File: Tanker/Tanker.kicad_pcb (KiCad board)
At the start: 2 copper layers, 47.6 x 18.8 mm, 1 part

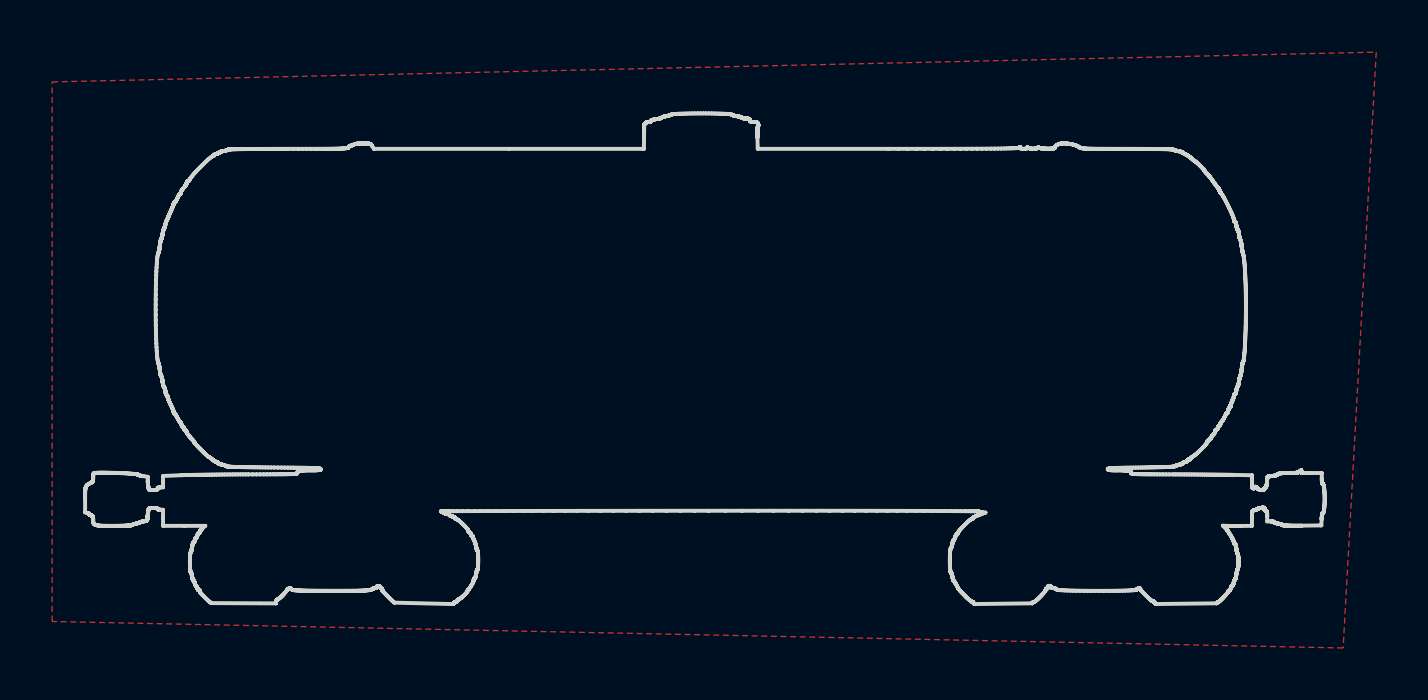
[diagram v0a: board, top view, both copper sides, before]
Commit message: Add & Align Pins
Add pins to all trains and set proper locations
Move RGB LEDs and resistors
Connect RGB LEDs to resistors and speaker to Arduino
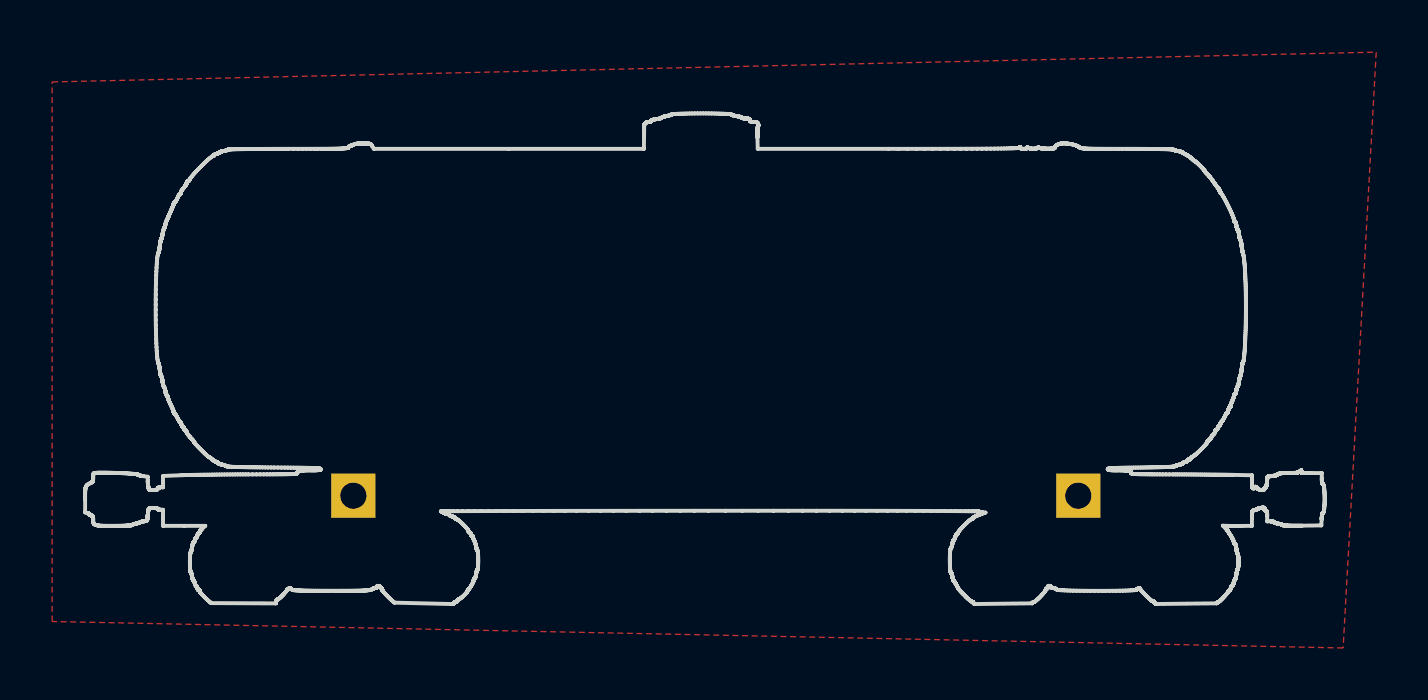
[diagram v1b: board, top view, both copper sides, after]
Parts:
- added MK1: Mounting_Hole_PAD, Pin_Headers:Pin_Header_Angled_1x01_Pitch2.54mm, B.Cu at (10.3, 95.8)
- added MK2: Mounting_Hole_PAD, Pin_Headers:Pin_Header_Angled_1x01_Pitch2.54mm, B.Cu at (38.1, 95.8)
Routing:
- added copper zone on F.Cu, net Net-(MK2-Pad1)
- removed copper zone on F.Cu, net (none)
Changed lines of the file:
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@@
-(kicad_pcb (version 20171130) (host pcbnew 5.0.0-rc2-dev-unknown-bf135b0~64~ubuntu16.04.1)
+(kicad_pcb (version 20171130) (host pcbnew 5.0.0-rc2-dev-unknown-1ac905d~64~ubuntu16.04.1)
   (general
     (thickness 1.6)
@@
     (tracks 0)
     (zones 0)
-    (modules 1)
-    (nets 1)
+    (modules 3)
+    (nets 2)
   )
   (page A4)
@@
   )
   (net 0 "")
+  (net 1 "Net-(MK2-Pad1)")
   (net_class Default "This is the default net class."
     (clearance 0.2)
@@
       (xy -1.887905 -6.02479) (xy -0.5608 -6.024797) (xy 0.777796 -6.024789)) (layer F.Mask) (width 0.01))
   )
+  (module Pin_Headers:Pin_Header_Angled_1x01_Pitch2.54mm (layer B.Cu)
+    (at 10.287 95.758 270)
+    (descr "Through hole angled pin header, 1x01, 2.54mm pitch, 6mm pin length, single row")
+    (tags "Through hole angled pin header THT 1x01 2.54mm single row")
+    (fp_text reference MK1 (at 4.385 2.27 270) (layer B.SilkS) hide
+      (effects (font (size 1 1) (thickness 0.15)) (justify mirror))
+    )
+    (fp_text value Mounting_Hole_PAD (at 4.385 -2.27 270) (layer B.Fab)
+      (effects (font (size 1 1) (thickness 0.15)) (justify mirror))
+    )
+    (fp_line (start 2.135 1.27) (end 4.04 1.27) (layer B.Fab) (width 0.1))
+    (fp_line (start 4.04 1.27) (end 4.04 -1.27) (layer B.Fab) (width 0.1))
+    (fp_line (start 4.04 -1.27) (end 1.5 -1.27) (layer B.Fab) (width 0.1))
+    (fp_line (start 1.5 -1.27) (end 1.5 0.635) (layer B.Fab) (width 0.1))
+    (fp_line (start 1.5 0.635) (end 2.135 1.27) (layer B.Fab) (width 0.1))
+    (fp_line (start -0.32 0.32) (end 1.5 0.32) (layer B.Fab) (width 0.1))
+    (fp_line (start -0.32 0.32) (end -0.32 -0.32) (layer B.Fab) (width 0.1))
+    (fp_line (start -0.32 -0.32) (end 1.5 -0.32) (layer B.Fab) (width 0.1))
+    (fp_line (start 4.04 0.32) (end 10.04 0.32) (layer B.Fab) (width 0.1))
+    (fp_line (start 10.04 0.32) (end 10.04 -0.32) (layer B.Fab) (width 0.1))
+    (fp_line (start 4.04 -0.32) (end 10.04 -0.32) (layer B.Fab) (width 0.1))
+    (fp_line (start 1.44 1.33) (end 1.44 -1.33) (layer B.SilkS) (width 0.12))
+    (fp_line (start 1.44 -1.33) (end 4.1 -1.33) (layer B.SilkS) (width 0.12))
+    (fp_line (start 4.1 -1.33) (end 4.1 1.33) (layer B.SilkS) (width 0.12))
+    (fp_line (start 4.1 1.33) (end 1.44 1.33) (layer B.SilkS) (width 0.12))
+    (fp_line (start 4.1 0.38) (end 10.1 0.38) (layer B.SilkS) (width 0.12))
+    (fp_line (start 10.1 0.38) (end 10.1 -0.38) (layer B.SilkS) (width 0.12))
+    (fp_line (start 10.1 -0.38) (end 4.1 -0.38) (layer B.SilkS) (width 0.12))
+    (fp_line (start 4.1 0.32) (end 10.1 0.32) (layer B.SilkS) (width 0.12))
+    (fp_line (start 4.1 0.2) (end 10.1 0.2) (layer B.SilkS) (width 0.12))
+    (fp_line (start 4.1 0.08) (end 10.1 0.08) (layer B.SilkS) (width 0.12))
+    (fp_line (start 4.1 -0.04) (end 10.1 -0.04) (layer B.SilkS) (width 0.12))
+    (fp_line (start 4.1 -0.16) (end 10.1 -0.16) (layer B.SilkS) (width 0.12))
+    (fp_line (start 4.1 -0.28) (end 10.1 -0.28) (layer B.SilkS) (width 0.12))
+    (fp_line (start 1.11 0.38) (end 1.44 0.38) (layer B.SilkS) (width 0.12))
+    (fp_line (start 1.11 -0.38) (end 1.44 -0.38) (layer B.SilkS) (width 0.12))
+    (fp_line (start -1.27 0) (end -1.27 1.27) (layer B.SilkS) (width 0.12))
+    (fp_line (start -1.27 1.27) (end 0 1.27) (layer B.SilkS) (width 0.12))
+    (fp_line (start -1.8 1.8) (end -1.8 -1.8) (layer B.CrtYd) (width 0.05))
+    (fp_line (start -1.8 -1.8) (end 10.55 -1.8) (layer B.CrtYd) (width 0.05))
+    (fp_line (start 10.55 -1.8) (end 10.55 1.8) (layer B.CrtYd) (width 0.05))
+    (fp_line (start 10.55 1.8) (end -1.8 1.8) (layer B.CrtYd) (width 0.05))
+    (fp_text user %R (at 2.77 0 180) (layer B.Fab)
+      (effects (font (size 1 1) (thickness 0.15)) (justify mirror))
+    )
+    (pad 1 thru_hole rect (at 0 0 270) (size 1.7 1.7) (drill 1) (layers *.Cu *.Mask))
+    (model ${KISYS3DMOD}/Pin_Headers.3dshapes/Pin_Header_Angled_1x01_Pitch2.54mm.wrl
+      (at (xyz 0 0 0))
+      (scale (xyz 1 1 1))
+      (rotate (xyz 0 0 0))
+    )
+  )
+  (module Pin_Headers:Pin_Header_Angled_1x01_Pitch2.54mm (layer B.Cu)
+    (at 38.1 95.758 270)
+    (descr "Through hole angled pin header, 1x01, 2.54mm pitch, 6mm pin length, single row")
+    (tags "Through hole angled pin header THT 1x01 2.54mm single row")
+    (fp_text reference MK2 (at 4.385 2.27 270) (layer B.SilkS) hide
+      (effects (font (size 1 1) (thickness 0.15)) (justify mirror))
+    )
+    (fp_text value Mounting_Hole_PAD (at 4.385 -2.27 270) (layer B.Fab)
+      (effects (font (size 1 1) (thickness 0.15)) (justify mirror))
+    )
+    (fp_text user %R (at 2.77 0 180) (layer B.Fab)
+      (effects (font (size 1 1) (thickness 0.15)) (justify mirror))
+    )
+    (fp_line (start 10.55 1.8) (end -1.8 1.8) (layer B.CrtYd) (width 0.05))
+    (fp_line (start 10.55 -1.8) (end 10.55 1.8) (layer B.CrtYd) (width 0.05))
+    (fp_line (start -1.8 -1.8) (end 10.55 -1.8) (layer B.CrtYd) (width 0.05))
+    (fp_line (start -1.8 1.8) (end -1.8 -1.8) (layer B.CrtYd) (width 0.05))
+    (fp_line (start -1.27 1.27) (end 0 1.27) (layer B.SilkS) (width 0.12))
+    (fp_line (start -1.27 0) (end -1.27 1.27) (layer B.SilkS) (width 0.12))
+    (fp_line (start 1.11 -0.38) (end 1.44 -0.38) (layer B.SilkS) (width 0.12))
+    (fp_line (start 1.11 0.38) (end 1.44 0.38) (layer B.SilkS) (width 0.12))
+    (fp_line (start 4.1 -0.28) (end 10.1 -0.28) (layer B.SilkS) (width 0.12))
+    (fp_line (start 4.1 -0.16) (end 10.1 -0.16) (layer B.SilkS) (width 0.12))
+    (fp_line (start 4.1 -0.04) (end 10.1 -0.04) (layer B.SilkS) (width 0.12))
+    (fp_line (start 4.1 0.08) (end 10.1 0.08) (layer B.SilkS) (width 0.12))
+    (fp_line (start 4.1 0.2) (end 10.1 0.2) (layer B.SilkS) (width 0.12))
+    (fp_line (start 4.1 0.32) (end 10.1 0.32) (layer B.SilkS) (width 0.12))
+    (fp_line (start 10.1 -0.38) (end 4.1 -0.38) (layer B.SilkS) (width 0.12))
+    (fp_line (start 10.1 0.38) (end 10.1 -0.38) (layer B.SilkS) (width 0.12))
+    (fp_line (start 4.1 0.38) (end 10.1 0.38) (layer B.SilkS) (width 0.12))
+    (fp_line (start 4.1 1.33) (end 1.44 1.33) (layer B.SilkS) (width 0.12))
+    (fp_line (start 4.1 -1.33) (end 4.1 1.33) (layer B.SilkS) (width 0.12))
+    (fp_line (start 1.44 -1.33) (end 4.1 -1.33) (layer B.SilkS) (width 0.12))
+    (fp_line (start 1.44 1.33) (end 1.44 -1.33) (layer B.SilkS) (width 0.12))
+    (fp_line (start 4.04 -0.32) (end 10.04 -0.32) (layer B.Fab) (width 0.1))
+    (fp_line (start 10.04 0.32) (end 10.04 -0.32) (layer B.Fab) (width 0.1))
+    (fp_line (start 4.04 0.32) (end 10.04 0.32) (layer B.Fab) (width 0.1))
+    (fp_line (start -0.32 -0.32) (end 1.5 -0.32) (layer B.Fab) (width 0.1))
+    (fp_line (start -0.32 0.32) (end -0.32 -0.32) (layer B.Fab) (width 0.1))
+    (fp_line (start -0.32 0.32) (end 1.5 0.32) (layer B.Fab) (width 0.1))
+    (fp_line (start 1.5 0.635) (end 2.135 1.27) (layer B.Fab) (width 0.1))
+    (fp_line (start 1.5 -1.27) (end 1.5 0.635) (layer B.Fab) (width 0.1))
+    (fp_line (start 4.04 -1.27) (end 1.5 -1.27) (layer B.Fab) (width 0.1))
+    (fp_line (start 4.04 1.27) (end 4.04 -1.27) (layer B.Fab) (width 0.1))
+    (fp_line (start 2.135 1.27) (end 4.04 1.27) (layer B.Fab) (width 0.1))
+    (pad 1 thru_hole rect (at 0 0 270) (size 1.7 1.7) (drill 1) (layers *.Cu *.Mask))
+    (model ${KISYS3DMOD}/Pin_Headers.3dshapes/Pin_Header_Angled_1x01_Pitch2.54mm.wrl
+      (at (xyz 0 0 0))
+      (scale (xyz 1 1 1))
+      (rotate (xyz 0 0 0))
+    )
+  )
   (gr_line (start 40.809031 94.673487) (end 40.735042 94.674473) (layer Edge.Cuts) (width 0.15))
   (gr_line (start 40.88027 94.672451) (end 40.809031 94.673487) (layer Edge.Cuts) (width 0.15))
@@
   (gr_line (start 3.807543 93.216175) (end 3.805144 93.21425) (layer Edge.Cuts) (width 0.15))
   (gr_line (start 3.81 93.218) (end 3.807543 93.216175) (layer Edge.Cuts) (width 0.15))
-  (zone (net 0) (net_name "") (layer F.Cu) (hatch edge 0.508)
+  (zone (net 1) (net_name "Net-(MK2-Pad1)") (layer F.Cu) (hatch edge 0.508)
     (connect_pads (clearance 0.508))
     (min_thickness 0.254)
